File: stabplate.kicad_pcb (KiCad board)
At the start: 2 copper layers, 146.1 x 82.5 mm, 7 parts, among them SW1 SW_Push, SW2 SW_Push, SW3 SW_Push, SW4 SW_Push, SW5 SW_Push, SW6 SW_Push, SW7 SW_Push

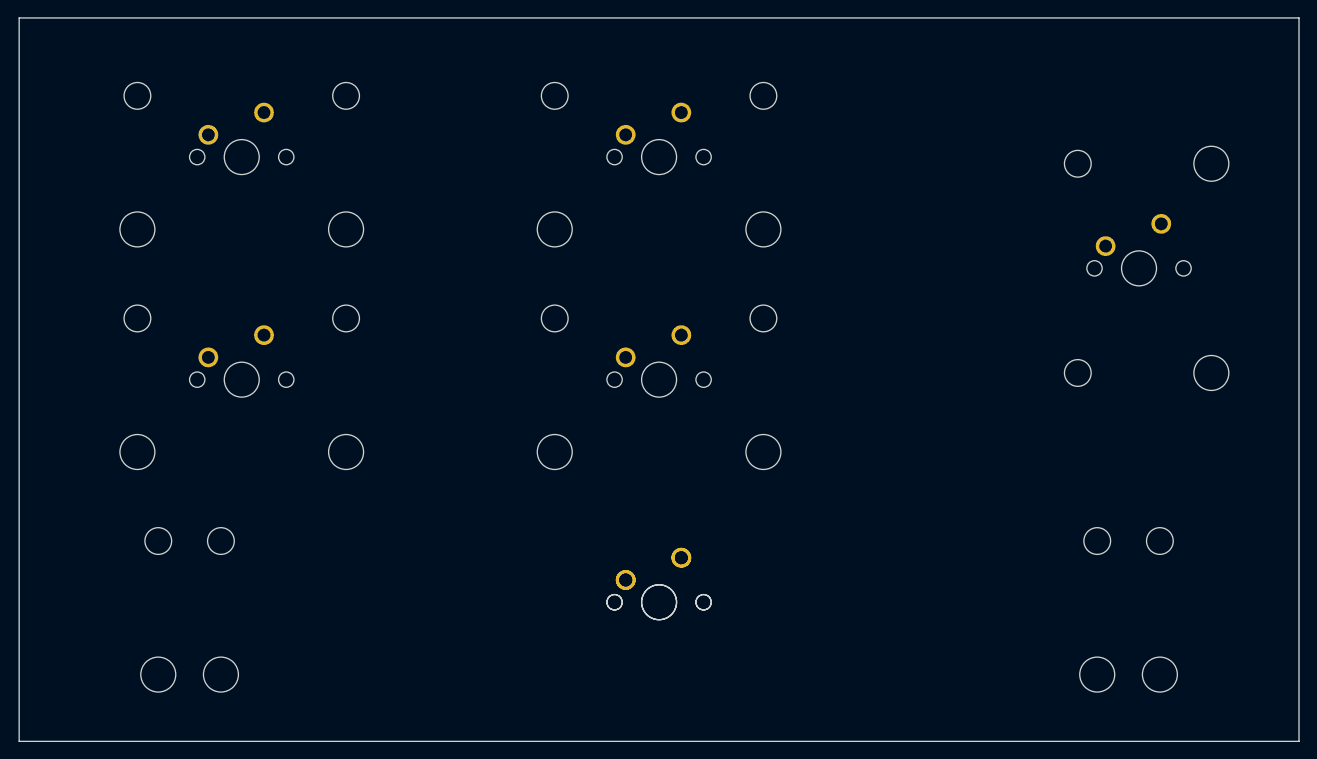
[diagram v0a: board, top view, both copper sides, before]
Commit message: changed to 2.75u, added copper planes
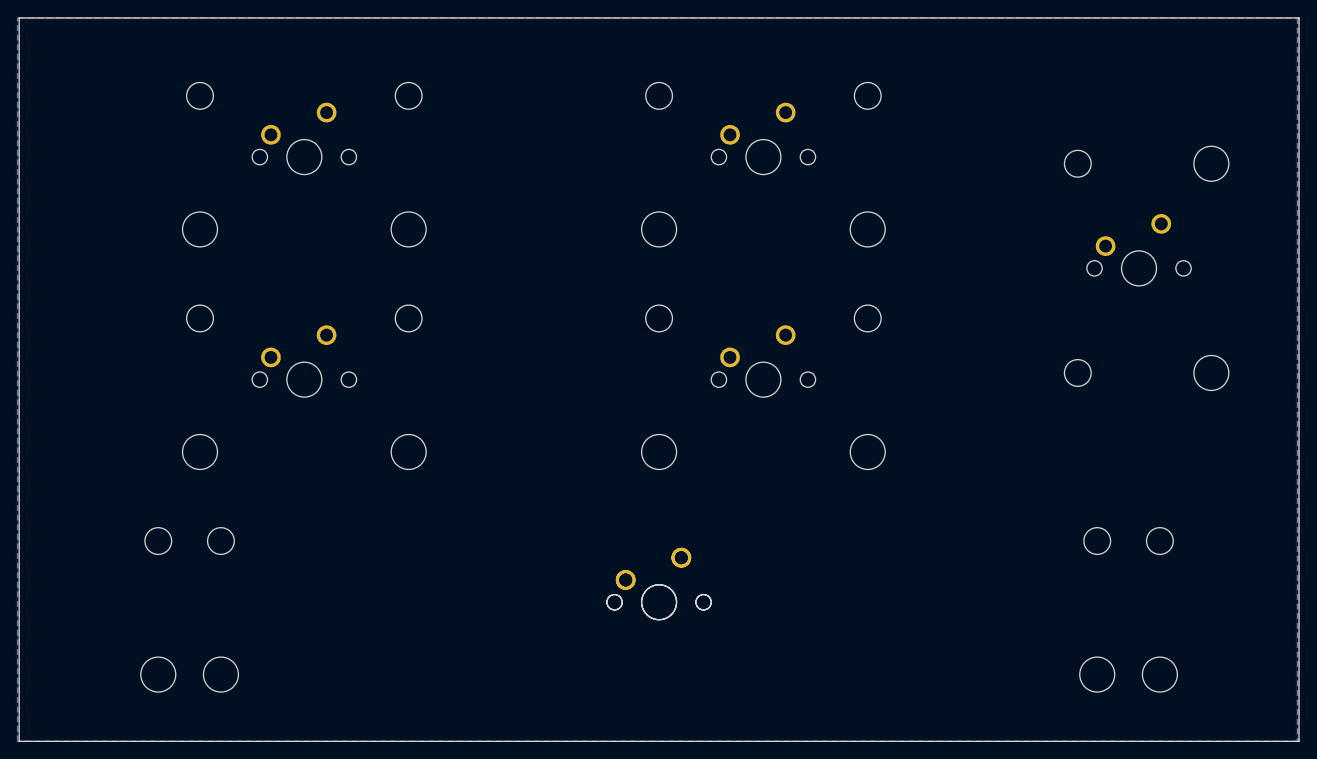
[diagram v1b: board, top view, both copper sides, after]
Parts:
- SW1, SW2, SW3, SW4: footprint MX_Only:MXOnly-2U-NoLED -> MX_Only:MXOnly-2.75U-NoLED
- moved SW2 11.9 mm to (164.3, 126.2)
- moved SW3 11.9 mm to (164.3, 100.8)
- moved SW1 7.14 mm to (111.9, 100.8)
- moved SW4 7.14 mm to (111.9, 126.2)
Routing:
- added copper zone on B.Cu, net (none)
- added copper zone on F.Cu, net (none)
